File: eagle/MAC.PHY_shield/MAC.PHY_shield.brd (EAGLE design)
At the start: 52.8 x 35.2 mm, 21 parts, among them IC1 ENC28J60, Q1 CSM-7X-DU

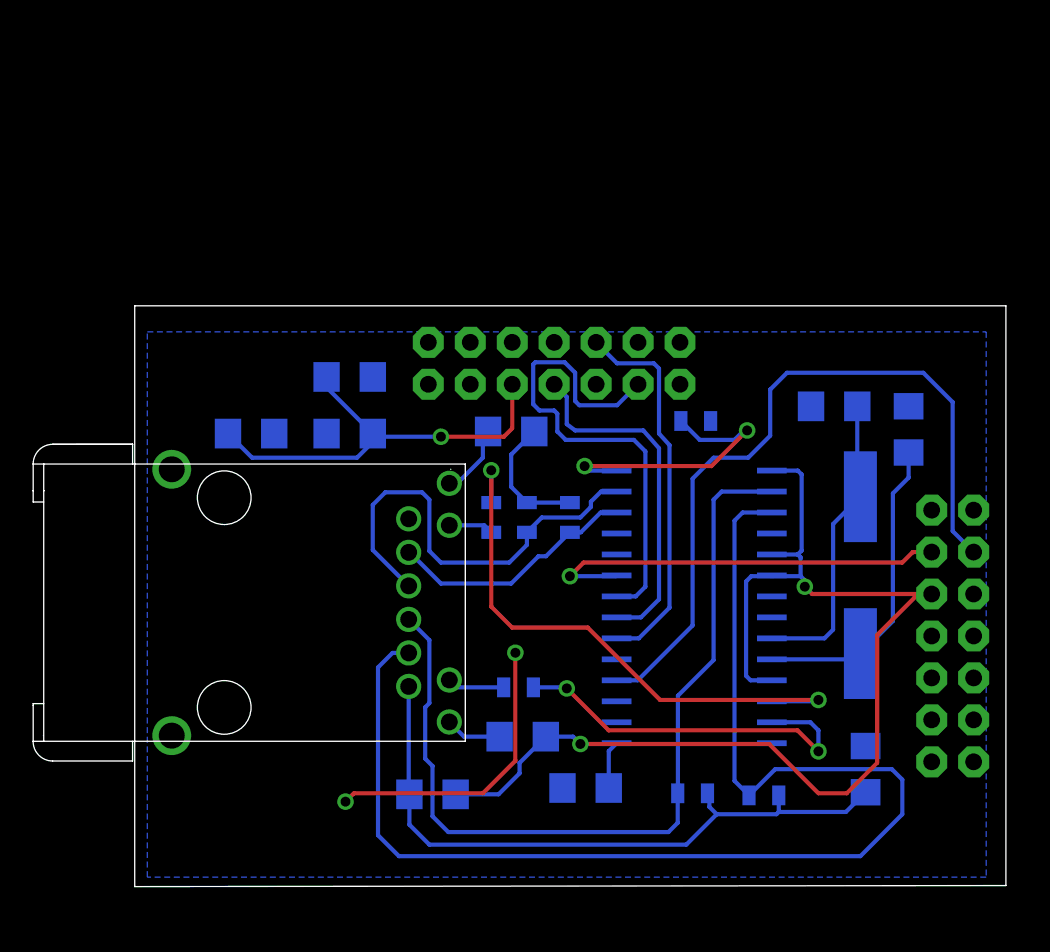
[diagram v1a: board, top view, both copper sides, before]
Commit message: Changed ENC board
Signed-off-by: Pavlo Manovi <pavlo.manovi@gmail.com>
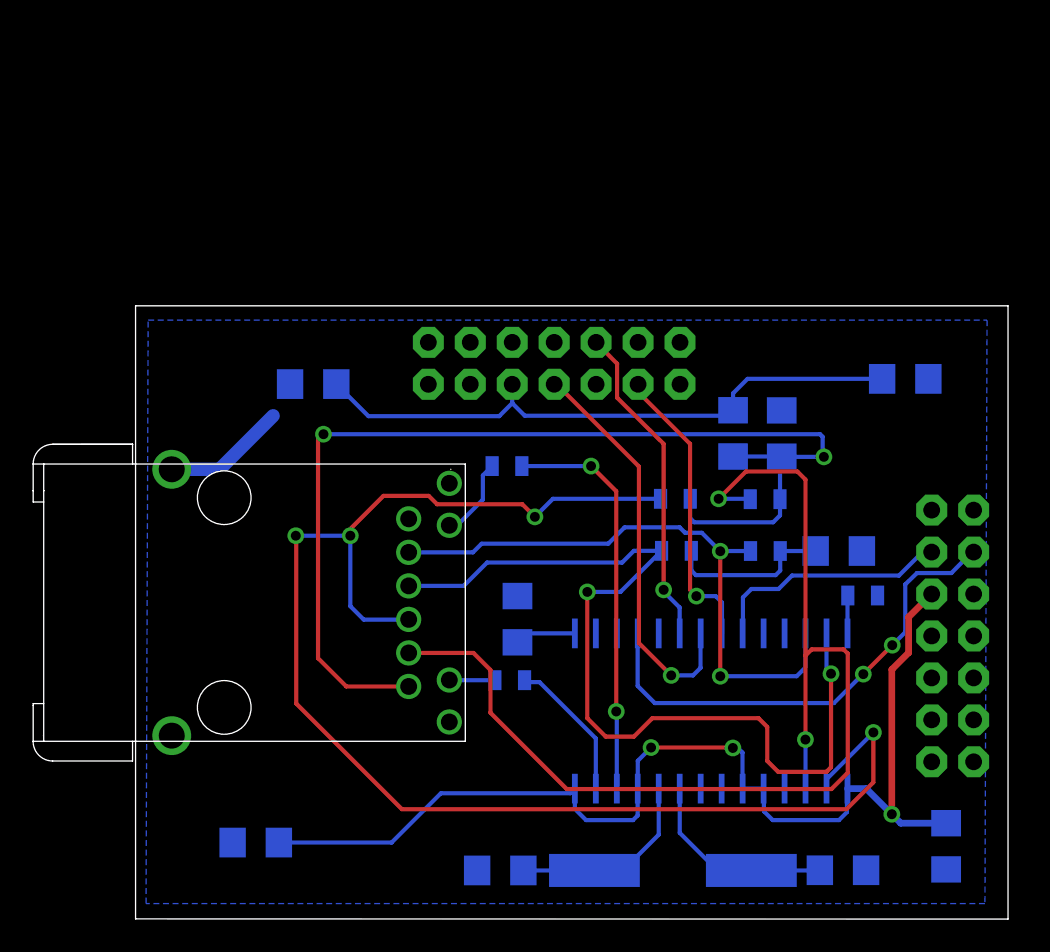
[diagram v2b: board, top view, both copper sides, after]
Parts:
- moved C8 46.0 mm to (56.0, 12.0), turned to 90 degrees
- moved C6 36.4 mm to (29.0, 10.6), turned to 0 degrees
- moved C7 31.7 mm to (53.5, 40.3), turned to 0 degrees
- moved U$4 28.4 mm to (43.1, 37.0), turned to 270 degrees
- moved C5 28.1 mm to (49.7, 10.6), turned to 180 degrees
- moved C10 24.8 mm to (14.2, 12.3), turned to 0 degrees
- moved Q1 21.2 mm to (39.4, 10.6), turned to 180 degrees
- moved C4 21.1 mm to (49.5, 29.9), turned to 180 degrees
- moved C3 20.9 mm to (46.0, 37.0)
- moved R4 17.9 mm to (45.0, 33.0)
- moved R5 17.9 mm to (39.6, 33.1)
- moved R8 14.6 mm to (50.9, 27.2)
- moved R7 12.0 mm to (45.0, 29.9), turned to 0 degrees
- moved C2 11.0 mm to (30.0, 25.8), turned to 90 degrees
- moved R6 9.28 mm to (39.7, 29.9), turned to 180 degrees
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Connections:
- net VCC3V3: now also IC1.P$28
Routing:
- net N$6: track 52.4 -> 88.5 mm, vias 0 -> 4
- net N$7: track 26.9 -> 55.9 mm, vias 0 -> 2
- net N$4: track 40.3 -> 67.4 mm, vias 0 -> 2
- net N$9: track 15.2 -> 36.9 mm, vias 0 -> 2
- net GND: track 25.7 -> 7.48 mm, vias 2 -> 0
- net N$17: track 45.2 -> 29.4 mm, vias 0 -> 2
- net N$11: track 17.5 -> 2.30 mm, vias 2 -> 0
- net N$2: track 23.2 -> 8.81 mm, vias 2 -> 0
- net N$12: track 30.2 -> 17.9 mm, vias 0 -> 1
- net N$3: track 35.2 -> 24.4 mm
- net N$10: track 25.4 -> 14.8 mm, vias 1 -> 0
- net N$5: track 77.5 -> 68.8 mm, vias 0 -> 2
- net VCC3V3: track 96.3 -> 104.9 mm
- net N$14: track 18.9 -> 11.9 mm
- net N$13: track 18.2 -> 13.5 mm
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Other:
- board size 52.8 x 35.2 mm -> 52.8 x 37.1 mm

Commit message: Added Alumni Boards and new version of MAC.PHY shield
Signed-off-by: Pavlo Manovi <pavlo.manovi@gmail.com>
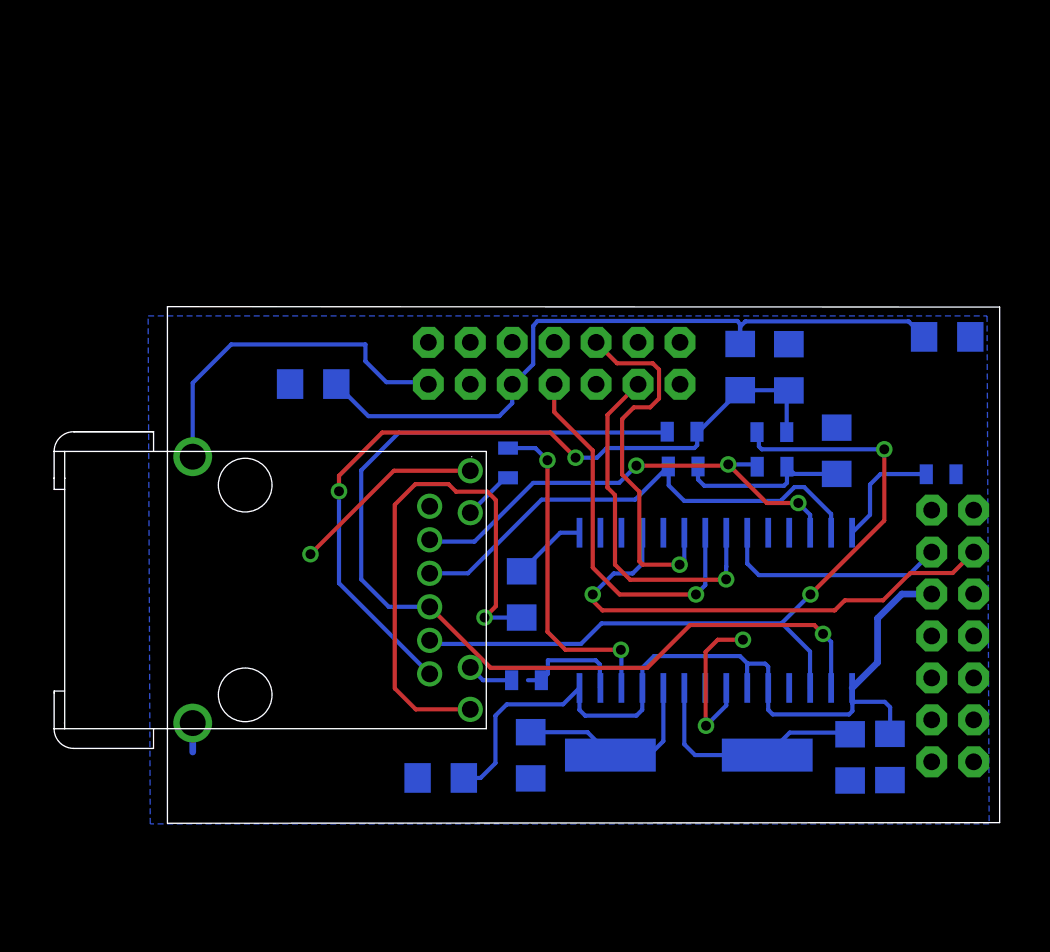
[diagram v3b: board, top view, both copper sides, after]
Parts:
- moved C10 11.9 mm to (25.4, 16.2)
- moved R8 8.74 mm to (55.7, 34.6)
- moved C6 7.21 mm to (30.8, 17.5), turned to 270 degrees
- moved Q1 7.05 mm to (40.4, 17.6)
- moved C5 6.85 mm to (50.2, 17.4), turned to 270 degrees
- moved C8 6.39 mm to (52.6, 17.4)
- moved IC1 6.10 mm to (42.2, 26.4)
- moved C4 6.07 mm to (49.4, 36.0), turned to 90 degrees
- moved R6 5.12 mm to (40.1, 35.0)
- moved R7 5.12 mm to (45.5, 35.0)
- moved R4 4.08 mm to (45.4, 37.1)
- moved R5 4.08 mm to (40.0, 37.1)
- moved C3 4.04 mm to (46.5, 41.0)
- moved U$4 4.04 mm to (43.5, 41.0)
- moved C7 3.59 mm to (56.1, 42.9)
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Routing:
- net GND: track 7.48 -> 77.6 mm, vias 0 -> 4
- net N$6: track 88.5 -> 61.1 mm, vias 4 -> 1
- net N$7: track 55.9 -> 30.7 mm, vias 2 -> 0
- net N$5: track 68.8 -> 48.2 mm
- net N$4: track 67.4 -> 48.6 mm
- net VCC3V3: track 104.9 -> 95.4 mm, vias 3 -> 0
- net N$9: track 36.9 -> 29.2 mm, vias 2 -> 3
- net N$11: track 2.30 -> 7.04 mm
- net N$3: track 24.4 -> 20.3 mm
- net N$12: track 17.9 -> 21.8 mm
- net N$15: track 19.7 -> 22.6 mm
- net N$2: track 8.81 -> 6.87 mm
- net LEDB: track 4.94 -> 3.16 mm
- net N$16: track 24.7 -> 23.0 mm
- net N$17: track 29.4 -> 30.8 mm, vias 2 -> 1
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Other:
- board size 52.8 x 37.1 mm -> 50.4 x 31.3 mm

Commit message: Changes to bldc 4-layer. Finished ethershield v3.
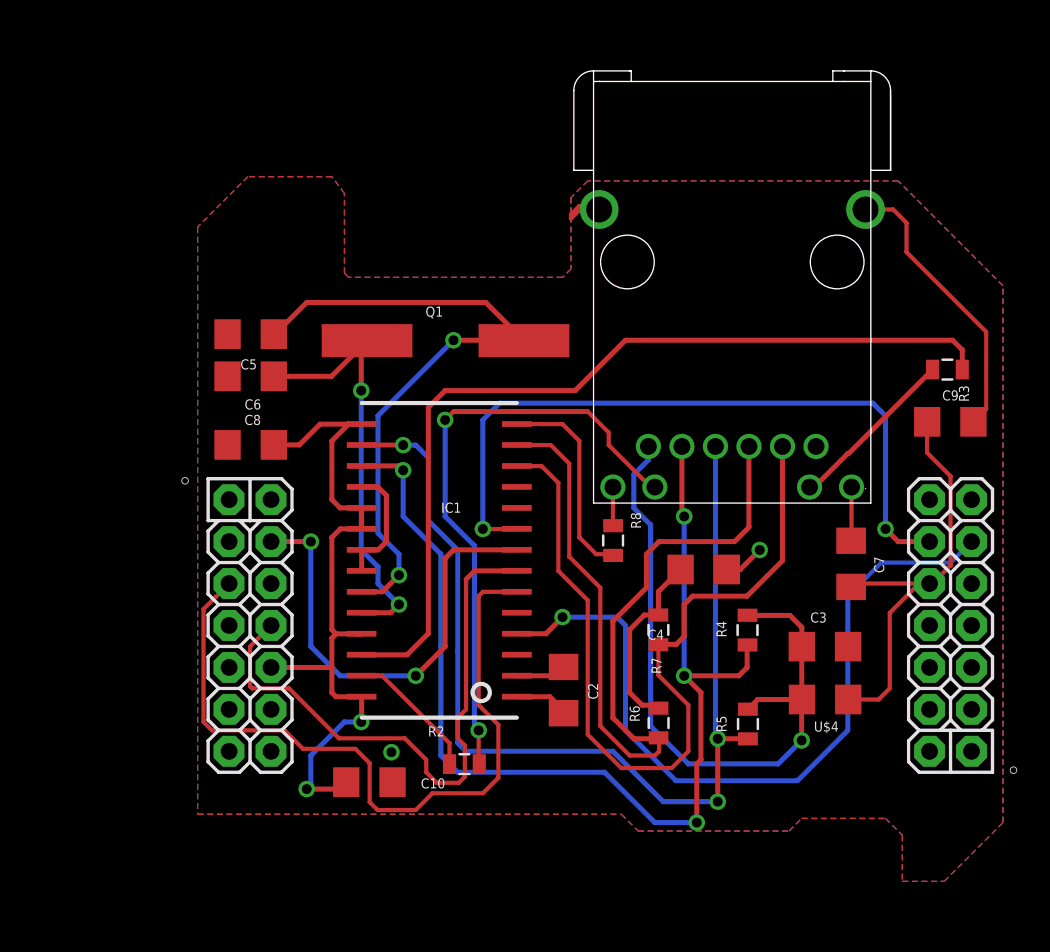
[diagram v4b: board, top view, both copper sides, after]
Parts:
- U$1: value CAN_NODE_SHIELD -> CANODE_SHIELD; device ASL:CAN_NODE_SHIELD -> ASL:CANODE_SHIELD
- moved C5 44.4 mm to (13.9, 43.0), flipped to the top, turned to 180 degrees
- moved C8 43.1 mm to (13.9, 36.3), flipped to the top, turned to 0 degrees
- moved C9 38.7 mm to (56.2, 37.7), flipped to the top
- moved Q1 29.1 mm to (25.7, 42.6), flipped to the top, turned to 0 degrees
- moved C6 28.5 mm to (13.9, 40.5), flipped to the top, turned to 180 degrees
- moved R3 27.2 mm to (56.1, 40.9), flipped to the top, turned to 0 degrees
- moved U$4 20.8 mm to (48.7, 20.9), flipped to the top, turned to 180 degrees
- moved R8 20.3 mm to (35.8, 30.5), flipped to the top, turned to 270 degrees
- moved R5 18.1 mm to (44.0, 19.4), flipped to the top, turned to 270 degrees
- moved IC1 17.1 mm to (25.4, 29.5), flipped to the top, turned to 180 degrees
- moved C3 17.1 mm to (48.7, 24.1), flipped to the top, turned to 0 degrees
- moved U$3 16.0 mm to (35.8, 33.8), turned to 0 degrees
- moved R6 15.6 mm to (38.6, 19.5), flipped to the top, turned to 90 degrees
- moved C7 14.9 mm to (50.2, 29.1), flipped to the top, turned to 270 degrees
- moved R4 12.1 mm to (44.0, 25.1), flipped to the top, turned to 90 degrees
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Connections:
- net GND: now also U$1.GND, U$1.GND1, U$1.GND2, U$1.GND3, U$1.GND4, U$1.GND5, U$1.GND6, U$1.GND7; no longer U$1.P$1, U$1.P$13, U$1.P$14, U$1.P$15, U$1.P$16, U$1.P$2, U$1.P$27, U$1.P$28
- net N$10: now also U$1.RB15; no longer U$1.P$12
- net N$12: now also U$1.RB9; no longer U$1.P$18
- net N$15: now also U$1.RB10; no longer U$1.P$19
- net N$16: now also U$1.RB8; no longer U$1.P$22
- net N$17: now also U$1.RB14; no longer U$1.P$11
- net RA2: now also U$1.RA2; no longer U$1.P$21
- net RB12: now also U$1.RB12; no longer U$1.P$17
- net VCC3V3: now also U$1.3V3, U$1.3V31; no longer U$1.P$10, U$1.P$24
- net VCC5V5: now also U$1.5V; no longer U$1.P$6
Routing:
- net GND: track 77.6 -> 35.8 mm, vias 4 -> 2
- net LEDA: track 2.81 -> 36.9 mm, vias 0 -> 2
- net N$3: track 20.3 -> 53.7 mm, vias 2 -> 0
- net N$10: track 13.9 -> 43.6 mm, vias 0 -> 2
- net VCC3V3: track 95.4 -> 69.0 mm, vias 0 -> 2
- net N$13: track 14.3 -> 40.5 mm, vias 0 -> 2
- net N$15: track 22.6 -> 45.2 mm, vias 1 -> 0
- net N$9: track 29.2 -> 51.2 mm, vias 3 -> 0
- net N$7: track 30.7 -> 51.4 mm
- net N$5: track 48.2 -> 66.8 mm, vias 2 -> 4
- net N$17: track 30.8 -> 46.5 mm
- net N$14: track 12.2 -> 26.1 mm, vias 0 -> 2
- net N$16: track 23.0 -> 35.9 mm, vias 1 -> 0
- net LEDB: track 3.16 -> 10.4 mm
- net N$12: track 21.8 -> 28.3 mm, vias 1 -> 2
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- added copper zone on layer 1, net GND
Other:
- board size 50.4 x 31.3 mm -> 19.2 x 26.2 mm

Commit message: Completed BLDC 4-layer and new Ether-shield
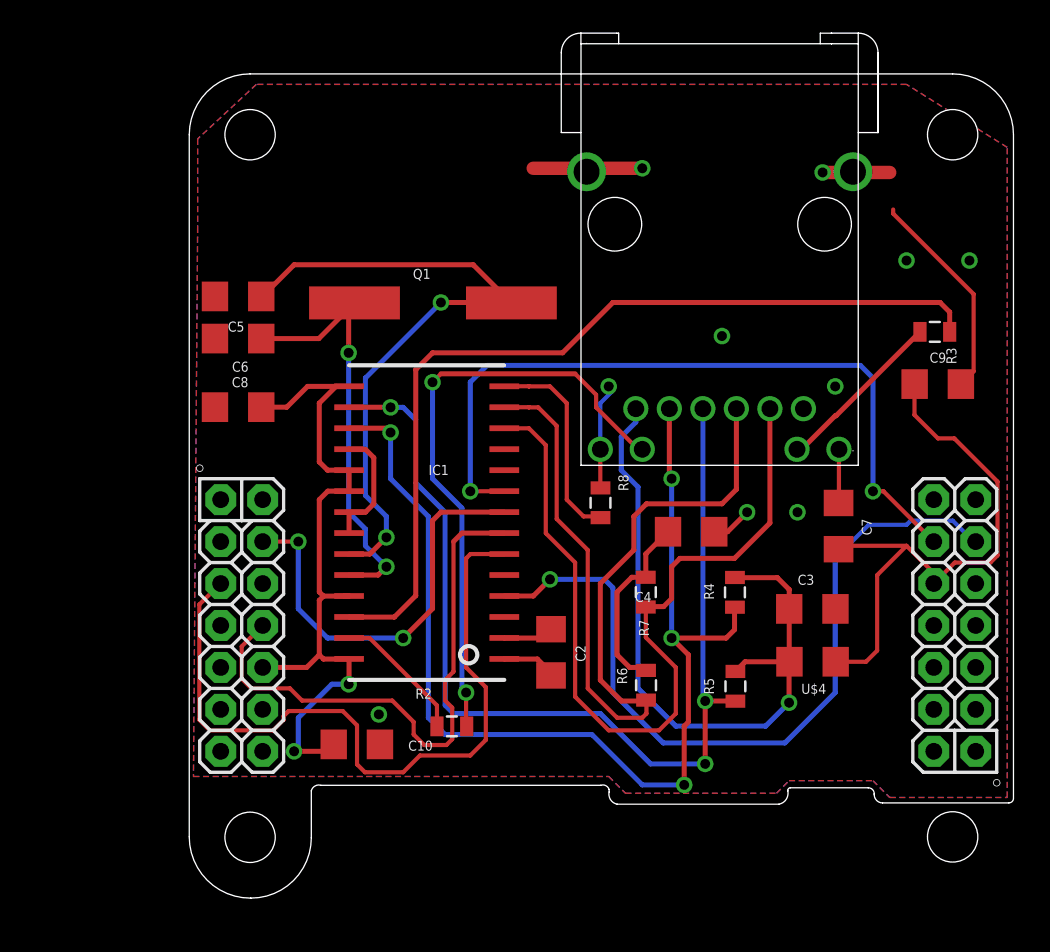
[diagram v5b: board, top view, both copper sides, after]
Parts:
- added E$1, E$2, E$3, E$4: (no value), ASL:STAND-OFF-TIGHT
- moved C2 2.41 mm to (32.1, 23.8)
- moved C3 2.41 mm to (47.9, 26.4)
- moved C5 2.41 mm to (13.1, 45.3)
- moved C6 2.41 mm to (13.1, 42.8)
- moved C8 2.41 mm to (13.1, 38.6)
- moved C9 2.41 mm to (55.5, 40.0)
- moved Q1 2.41 mm to (24.9, 44.9)
- moved R3 2.41 mm to (55.3, 43.2)
- moved R4 2.41 mm to (43.2, 27.4)
- moved R6 2.41 mm to (37.8, 21.8)
- moved R7 2.41 mm to (37.8, 27.4)
- moved R8 2.41 mm to (35.1, 32.8)
- moved U$3 2.41 mm to (35.1, 36.1)
- moved U$4 2.41 mm to (47.9, 23.2)
- moved C10 2.41 mm to (20.3, 18.2)
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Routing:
- net GND: track 35.8 -> 46.1 mm, vias 2 -> 10
- net VCC3V3: track 69.0 -> 78.0 mm
- net N$18: track 3.98 -> 0.00 mm
- net N$12: track 28.3 -> 25.7 mm
- net N$10: track 43.6 -> 45.6 mm
- net N$16: track 35.9 -> 34.4 mm
- net N$17: track 46.5 -> 47.5 mm
- net N$15: track 45.2 -> 44.7 mm
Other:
- board size 19.2 x 26.2 mm -> 49.9 x 49.9 mm
